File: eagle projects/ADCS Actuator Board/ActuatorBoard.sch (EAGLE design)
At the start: 147 parts, among them J19 TE_1-84953-1, J20 TE_1-84953-1, J21 TE_1-84953-1, U1 TVS991, U10 DRV10970_MOTOR_DRIVERDRV10970, U12 DRV10970_MOTOR_DRIVERDRV10970, U2 ADS7841E_2K5, U3 ADS7841E_2K5, U35 BD6210F-E2, U39 BD6210F-E2, U5 TVS991, U7 DRV10970_MOTOR_DRIVERDRV10970, U8 TVS991, U9 BD6210F-E2

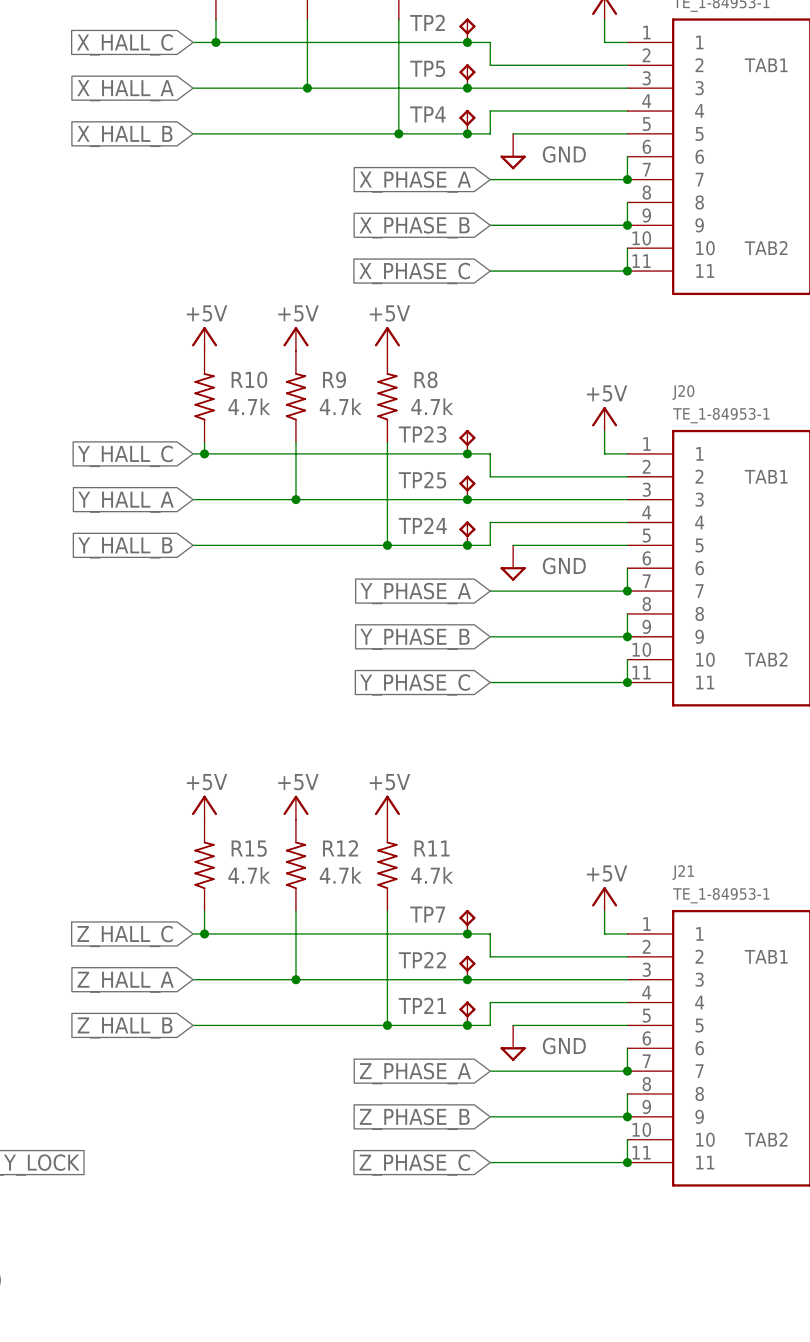
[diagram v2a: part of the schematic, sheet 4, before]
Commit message: Fixed wrong motor connector pinout
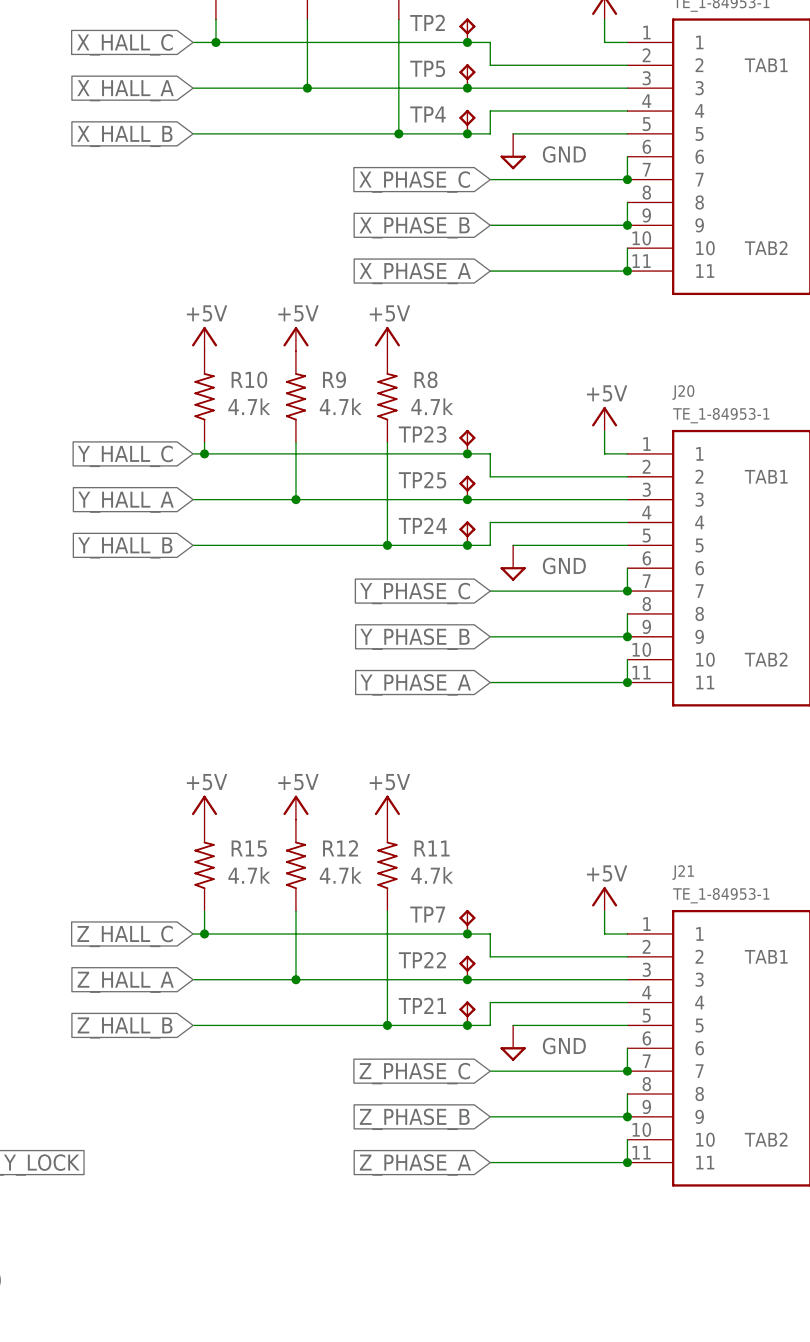
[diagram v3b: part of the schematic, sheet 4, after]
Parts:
- R3, R30, R4, R76: value 10k -> 5.1k
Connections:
- net X_PHASE_A: now also J19.10, J19.11; no longer J19.6, J19.7
- net X_PHASE_C: now also J19.6, J19.7; no longer J19.10, J19.11
- net Y_PHASE_A: now also J20.10, J20.11; no longer J20.6, J20.7
- net Y_PHASE_C: now also J20.6, J20.7; no longer J20.10, J20.11
- net Z_PHASE_A: now also J21.10, J21.11; no longer J21.6, J21.7
- net Z_PHASE_C: now also J21.6, J21.7; no longer J21.10, J21.11
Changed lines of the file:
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@@
 <part name="C123" library="rcl" library_urn="urn:adsk.eagle:library:334" deviceset="C-EU" device="C0402" package3d_urn="urn:adsk.eagle:package:23626/2" value="0.1u"/>
 <part name="SUPPLY185" library="supply2" library_urn="urn:adsk.eagle:library:372" deviceset="GND" device=""/>
-<part name="R30" library="rcl" library_urn="urn:adsk.eagle:library:334" deviceset="R-US_" device="R0402" package3d_urn="urn:adsk.eagle:package:23547/3" value="10k"/>
+<part name="R30" library="rcl" library_urn="urn:adsk.eagle:library:334" deviceset="R-US_" device="R0402" package3d_urn="urn:adsk.eagle:package:23547/3" value="5.1k"/>
 <part name="SUPPLY187" library="supply2" library_urn="urn:adsk.eagle:library:372" deviceset="GND" device=""/>
 <part name="U35" library="my_library" library_urn="urn:adsk.eagle:library:22876504" deviceset="BD6210F-E2" device="" package3d_urn="urn:adsk.eagle:package:24418978/3"/>
@@
 <part name="C131" library="rcl" library_urn="urn:adsk.eagle:library:334" deviceset="C-EU" device="C0402" package3d_urn="urn:adsk.eagle:package:23626/2" value="0.1u"/>
 <part name="SUPPLY197" library="supply2" library_urn="urn:adsk.eagle:library:372" deviceset="GND" device=""/>
-<part name="R76" library="rcl" library_urn="urn:adsk.eagle:library:334" deviceset="R-US_" device="R0402" package3d_urn="urn:adsk.eagle:package:23547/3" value="10k"/>
+<part name="R76" library="rcl" library_urn="urn:adsk.eagle:library:334" deviceset="R-US_" device="R0402" package3d_urn="urn:adsk.eagle:package:23547/3" value="5.1k"/>
 <part name="SUPPLY199" library="supply2" library_urn="urn:adsk.eagle:library:372" deviceset="GND" device=""/>
 <part name="U39" library="my_library" library_urn="urn:adsk.eagle:library:22876504" deviceset="BD6210F-E2" device="" package3d_urn="urn:adsk.eagle:package:24418978/3"/>
@@
 <part name="R22" library="rcl" library_urn="urn:adsk.eagle:library:334" deviceset="R-US_" device="M0805" package3d_urn="urn:adsk.eagle:package:23556/2"/>
 <part name="R23" library="rcl" library_urn="urn:adsk.eagle:library:334" deviceset="R-US_" device="M0805" package3d_urn="urn:adsk.eagle:package:23556/2"/>
-<part name="R3" library="rcl" library_urn="urn:adsk.eagle:library:334" deviceset="R-US_" device="R0402" package3d_urn="urn:adsk.eagle:package:23547/3" value="10k"/>
-<part name="R4" library="rcl" library_urn="urn:adsk.eagle:library:334" deviceset="R-US_" device="R0402" package3d_urn="urn:adsk.eagle:package:23547/3" value="10k"/>
+<part name="R3" library="rcl" library_urn="urn:adsk.eagle:library:334" deviceset="R-US_" device="R0402" package3d_urn="urn:adsk.eagle:package:23547/3" value="5.1k"/>
+<part name="R4" library="rcl" library_urn="urn:adsk.eagle:library:334" deviceset="R-US_" device="R0402" package3d_urn="urn:adsk.eagle:package:23547/3" value="5.1k"/>
 <part name="R5" library="rcl" library_urn="urn:adsk.eagle:library:334" deviceset="R-US_" device="R0402" package3d_urn="urn:adsk.eagle:package:23547/3" value="1.8k"/>
 <part name="R24" library="rcl" library_urn="urn:adsk.eagle:library:334" deviceset="R-US_" device="R0402" package3d_urn="urn:adsk.eagle:package:23547/3" value="1.8k"/>
@@
 <net name="Y_PHASE_C" class="0">
 <segment>
-<pinref part="J20" gate="G$1" pin="10"/>
-<pinref part="J20" gate="G$1" pin="11"/>
-<wire x1="236.22" y1="116.84" x2="236.22" y2="119.38" width="0.1524" layer="91"/>
-<label x="220.98" y="116.84" size="1.778" layer="95" rot="R180" xref="yes"/>
-<wire x1="236.22" y1="116.84" x2="220.98" y2="116.84" width="0.1524" layer="91"/>
-<junction x="236.22" y="116.84"/>
-</segment>
-<segment>
 <wire x1="76.2" y1="38.1" x2="73.66" y2="38.1" width="0.1524" layer="91"/>
 <wire x1="73.66" y1="38.1" x2="73.66" y2="30.48" width="0.1524" layer="91"/>
@@
 <pinref part="U7" gate="G$1" pin="W"/>
 </segment>
+<segment>
+<pinref part="J20" gate="G$1" pin="6"/>
+<pinref part="J20" gate="G$1" pin="7"/>
+<wire x1="236.22" y1="127" x2="236.22" y2="129.54" width="0.1524" layer="91"/>
+<label x="220.98" y="127" size="1.778" layer="95" rot="R180" xref="yes"/>
+<wire x1="236.22" y1="127" x2="220.98" y2="127" width="0.1524" layer="91"/>
+<junction x="236.22" y="127"/>
+</segment>
 </net>
 <net name="Y_PHASE_B" class="0">
@@
 <net name="Y_PHASE_A" class="0">
 <segment>
-<pinref part="J20" gate="G$1" pin="6"/>
-<pinref part="J20" gate="G$1" pin="7"/>
-<wire x1="236.22" y1="127" x2="236.22" y2="129.54" width="0.1524" layer="91"/>
-<label x="220.98" y="127" size="1.778" layer="95" rot="R180" xref="yes"/>
-<wire x1="236.22" y1="127" x2="220.98" y2="127" width="0.1524" layer="91"/>
-<junction x="236.22" y="127"/>
-</segment>
-<segment>
 <wire x1="114.3" y1="38.1" x2="111.76" y2="38.1" width="0.1524" layer="91"/>
 <wire x1="114.3" y1="38.1" x2="114.3" y2="17.78" width="0.1524" layer="91"/>
@@
 <wire x1="73.66" y1="17.78" x2="114.3" y2="17.78" width="0.1524" layer="91"/>
 </segment>
+<segment>
+<pinref part="J20" gate="G$1" pin="10"/>
+<pinref part="J20" gate="G$1" pin="11"/>
+<wire x1="236.22" y1="116.84" x2="236.22" y2="119.38" width="0.1524" layer="91"/>
+<label x="220.98" y="116.84" size="1.778" layer="95" rot="R180" xref="yes"/>
+<wire x1="236.22" y1="116.84" x2="220.98" y2="116.84" width="0.1524" layer="91"/>
+<junction x="236.22" y="116.84"/>
+</segment>
 </net>
 <net name="Z_PHASE_C" class="0">
@@
 </segment>
 <segment>
-<pinref part="J21" gate="G$1" pin="10"/>
-<pinref part="J21" gate="G$1" pin="11"/>
-<wire x1="236.22" y1="63.5" x2="236.22" y2="66.04" width="0.1524" layer="91"/>
-<label x="220.98" y="63.5" size="1.778" layer="95" rot="R180" xref="yes"/>
-<wire x1="236.22" y1="63.5" x2="220.98" y2="63.5" width="0.1524" layer="91"/>
-<junction x="236.22" y="63.5"/>
+<pinref part="J21" gate="G$1" pin="6"/>
+<pinref part="J21" gate="G$1" pin="7"/>
+<wire x1="236.22" y1="73.66" x2="236.22" y2="76.2" width="0.1524" layer="91"/>
+<label x="220.98" y="73.66" size="1.778" layer="95" rot="R180" xref="yes"/>
+<wire x1="236.22" y1="73.66" x2="220.98" y2="73.66" width="0.1524" layer="91"/>
+<junction x="236.22" y="73.66"/>
 </segment>
 </net>
@@
 </segment>
 <segment>
-<pinref part="J21" gate="G$1" pin="6"/>
-<pinref part="J21" gate="G$1" pin="7"/>
-<wire x1="236.22" y1="73.66" x2="236.22" y2="76.2" width="0.1524" layer="91"/>
-<label x="220.98" y="73.66" size="1.778" layer="95" rot="R180" xref="yes"/>
-<wire x1="236.22" y1="73.66" x2="220.98" y2="73.66" width="0.1524" layer="91"/>
-<junction x="236.22" y="73.66"/>
+<pinref part="J21" gate="G$1" pin="10"/>
+<pinref part="J21" gate="G$1" pin="11"/>
+<wire x1="236.22" y1="63.5" x2="236.22" y2="66.04" width="0.1524" layer="91"/>
+<label x="220.98" y="63.5" size="1.778" layer="95" rot="R180" xref="yes"/>
+<wire x1="236.22" y1="63.5" x2="220.98" y2="63.5" width="0.1524" layer="91"/>
+<junction x="236.22" y="63.5"/>
 </segment>
 </net>
@@
 <net name="X_PHASE_C" class="0">
 <segment>
-<pinref part="J19" gate="G$1" pin="10"/>
-<pinref part="J19" gate="G$1" pin="11"/>
-<wire x1="236.22" y1="162.56" x2="236.22" y2="165.1" width="0.1524" layer="91"/>
-<label x="220.98" y="162.56" size="1.778" layer="95" rot="R180" xref="yes"/>
-<wire x1="236.22" y1="162.56" x2="220.98" y2="162.56" width="0.1524" layer="91"/>
-<junction x="236.22" y="162.56"/>
+<pinref part="J19" gate="G$1" pin="6"/>
+<pinref part="J19" gate="G$1" pin="7"/>
+<wire x1="236.22" y1="175.26" x2="236.22" y2="172.72" width="0.1524" layer="91"/>
+<junction x="236.22" y="172.72"/>
+<label x="220.98" y="172.72" size="1.778" layer="95" rot="R180" xref="yes"/>
+<wire x1="236.22" y1="172.72" x2="220.98" y2="172.72" width="0.1524" layer="91"/>
 </segment>
 </net>
@@
 </segment>
 </net>
-<net name="X_PHASE_A" class="0">
-<segment>
-<pinref part="J19" gate="G$1" pin="6"/>
-<pinref part="J19" gate="G$1" pin="7"/>
-<wire x1="236.22" y1="175.26" x2="236.22" y2="172.72" width="0.1524" layer="91"/>
-<junction x="236.22" y="172.72"/>
-<label x="220.98" y="172.72" size="1.778" layer="95" rot="R180" xref="yes"/>
-<wire x1="236.22" y1="172.72" x2="220.98" y2="172.72" width="0.1524" layer="91"/>
-</segment>
-</net>
 <net name="X_HALL_C" class="0">
 <segment>
@@
 </segment>
 </net>
+<net name="X_PHASE_A" class="0">
+<segment>
+<pinref part="J19" gate="G$1" pin="10"/>
+<pinref part="J19" gate="G$1" pin="11"/>
+<wire x1="236.22" y1="162.56" x2="236.22" y2="165.1" width="0.1524" layer="91"/>
+<label x="220.98" y="162.56" size="1.778" layer="95" rot="R180" xref="yes"/>
+<wire x1="236.22" y1="162.56" x2="220.98" y2="162.56" width="0.1524" layer="91"/>
+<junction x="236.22" y="162.56"/>
+</segment>
+</net>
